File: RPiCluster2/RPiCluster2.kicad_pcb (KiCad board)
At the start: 2 copper layers, 100 x 100 mm, 85 parts, among them J1 RPi_slave_1, J10 Addr_1, J11 Addr_0, J2 RPi_slave_2, J3 RPi_slave_3, J4 RPi_slave_4, J5 Addr, J6 Power_header, J7 Signal_header, J8 Signal_socket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

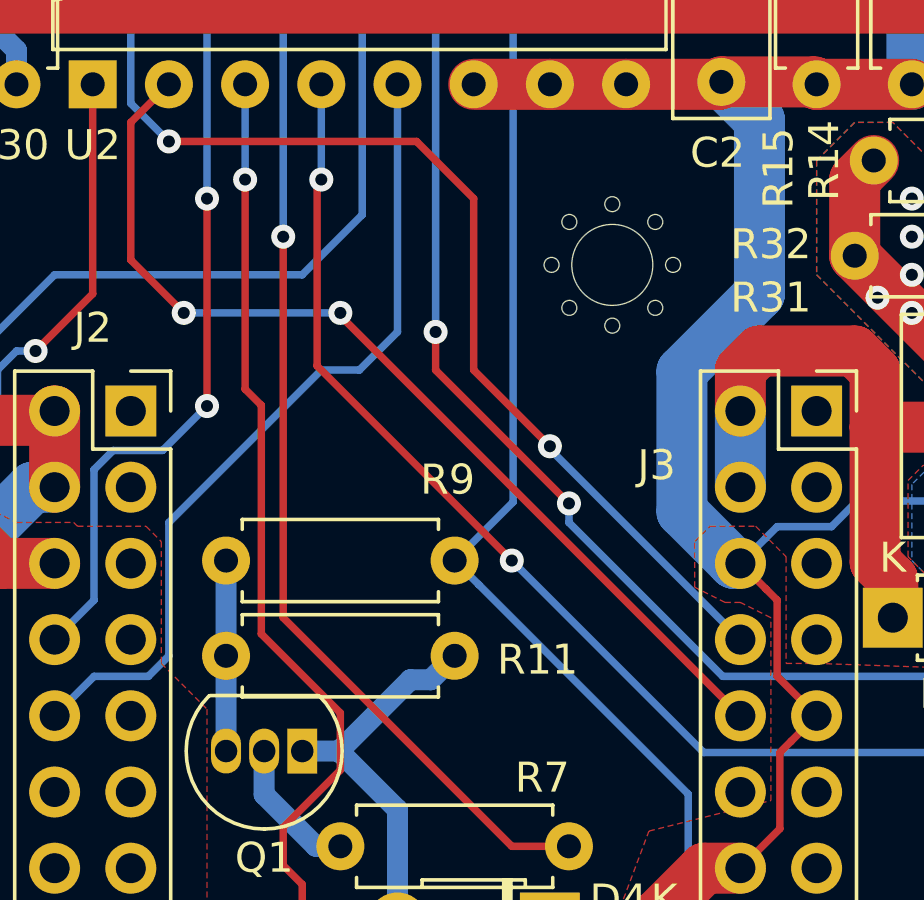
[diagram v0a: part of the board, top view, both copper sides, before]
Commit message: RPiCluster2: Avoid SER_EN from floating so that the board can be tested without MCP23008
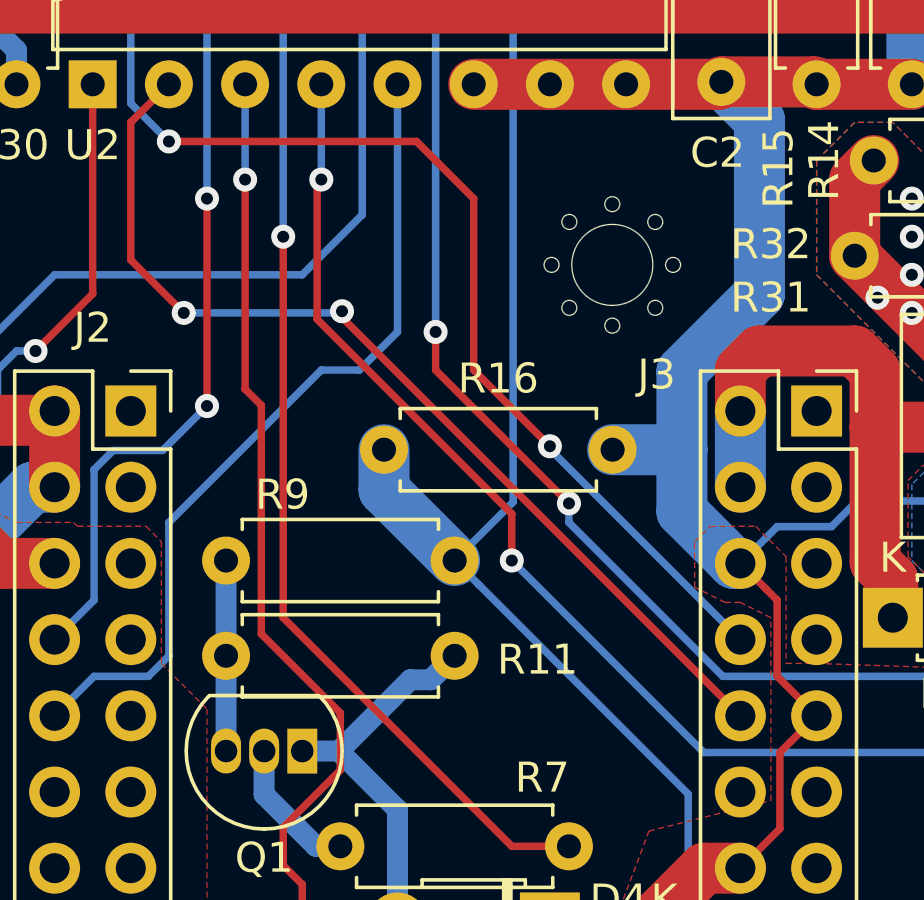
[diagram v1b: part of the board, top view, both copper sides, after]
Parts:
- added R16: 47k, Resistor_THT:R_Axial_DIN0207_L6.3mm_D2.5mm_P7.62mm_Horizontal, F.Cu at (99.9, 96.0)
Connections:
- J1 pad 1: (no net) -> Net-(J1-Pad1)
- J1 pad 11: (no net) -> Net-(J1-Pad11)
- J1 pad 12: (no net) -> Net-(J1-Pad12)
- J1 pad 13: (no net) -> Net-(J1-Pad13)
- J1 pad 15: (no net) -> Net-(J1-Pad15)
- J1 pad 16: (no net) -> Net-(J1-Pad16)
- J1 pad 17: (no net) -> Net-(J1-Pad17)
- J1 pad 18: (no net) -> Net-(J1-Pad18)
- J1 pad 19: (no net) -> Net-(J1-Pad19)
- J1 pad 21: (no net) -> Net-(J1-Pad21)
- J1 pad 22: (no net) -> Net-(J1-Pad22)
- J1 pad 23: (no net) -> Net-(J1-Pad23)
- J1 pad 24: (no net) -> Net-(J1-Pad24)
- J1 pad 26: (no net) -> Net-(J1-Pad26)
- J1 pad 27: (no net) -> Net-(J1-Pad27)
- J1 pad 28: (no net) -> Net-(J1-Pad28)
- J1 pad 29: (no net) -> Net-(J1-Pad29)
- J1 pad 3: (no net) -> Net-(J1-Pad3)
- J1 pad 31: (no net) -> Net-(J1-Pad31)
- J1 pad 32: (no net) -> Net-(J1-Pad32)
- J1 pad 33: (no net) -> Net-(J1-Pad33)
- J1 pad 35: (no net) -> Net-(J1-Pad35)
- J1 pad 36: (no net) -> Net-(J1-Pad36)
- J1 pad 37: (no net) -> Net-(J1-Pad37)
- J1 pad 38: (no net) -> Net-(J1-Pad38)
- J1 pad 40: (no net) -> Net-(J1-Pad40)
- J1 pad 5: (no net) -> Net-(J1-Pad5)
- J1 pad 7: (no net) -> Net-(J1-Pad7)
- J2 pad 1: (no net) -> Net-(J2-Pad1)
- J2 pad 11: (no net) -> Net-(J2-Pad11)
- J2 pad 12: (no net) -> Net-(J2-Pad12)
- J2 pad 13: (no net) -> Net-(J2-Pad13)
- J2 pad 15: (no net) -> Net-(J2-Pad15)
- J2 pad 16: (no net) -> Net-(J2-Pad16)
- J2 pad 17: (no net) -> Net-(J2-Pad17)
- J2 pad 18: (no net) -> Net-(J2-Pad18)
- J2 pad 19: (no net) -> Net-(J2-Pad19)
- J2 pad 21: (no net) -> Net-(J2-Pad21)
- J2 pad 22: (no net) -> Net-(J2-Pad22)
- J2 pad 23: (no net) -> Net-(J2-Pad23)
- J2 pad 24: (no net) -> Net-(J2-Pad24)
- J2 pad 26: (no net) -> Net-(J2-Pad26)
- J2 pad 27: (no net) -> Net-(J2-Pad27)
- J2 pad 28: (no net) -> Net-(J2-Pad28)
- J2 pad 29: (no net) -> Net-(J2-Pad29)
- J2 pad 3: (no net) -> Net-(J2-Pad3)
- J2 pad 31: (no net) -> Net-(J2-Pad31)
- J2 pad 32: (no net) -> Net-(J2-Pad32)
- J2 pad 33: (no net) -> Net-(J2-Pad33)
- J2 pad 35: (no net) -> Net-(J2-Pad35)
- J2 pad 36: (no net) -> Net-(J2-Pad36)
- J2 pad 37: (no net) -> Net-(J2-Pad37)
- J2 pad 38: (no net) -> Net-(J2-Pad38)
- J2 pad 40: (no net) -> Net-(J2-Pad40)
- J2 pad 5: (no net) -> Net-(J2-Pad5)
- J2 pad 7: (no net) -> Net-(J2-Pad7)
- J3 pad 1: (no net) -> Net-(J3-Pad1)
- J3 pad 11: (no net) -> Net-(J3-Pad11)
- J3 pad 12: (no net) -> Net-(J3-Pad12)
- J3 pad 13: (no net) -> Net-(J3-Pad13)
- J3 pad 15: (no net) -> Net-(J3-Pad15)
- J3 pad 16: (no net) -> Net-(J3-Pad16)
- J3 pad 17: (no net) -> Net-(J3-Pad17)
- J3 pad 18: (no net) -> Net-(J3-Pad18)
- J3 pad 19: (no net) -> Net-(J3-Pad19)
- J3 pad 21: (no net) -> Net-(J3-Pad21)
- J3 pad 22: (no net) -> Net-(J3-Pad22)
- J3 pad 23: (no net) -> Net-(J3-Pad23)
- J3 pad 24: (no net) -> Net-(J3-Pad24)
- J3 pad 26: (no net) -> Net-(J3-Pad26)
- J3 pad 27: (no net) -> Net-(J3-Pad27)
- J3 pad 28: (no net) -> Net-(J3-Pad28)
- J3 pad 29: (no net) -> Net-(J3-Pad29)
- J3 pad 3: (no net) -> Net-(J3-Pad3)
- J3 pad 31: (no net) -> Net-(J3-Pad31)
- J3 pad 32: (no net) -> Net-(J3-Pad32)
- J3 pad 33: (no net) -> Net-(J3-Pad33)
- J3 pad 35: (no net) -> Net-(J3-Pad35)
- J3 pad 36: (no net) -> Net-(J3-Pad36)
- J3 pad 37: (no net) -> Net-(J3-Pad37)
- J3 pad 38: (no net) -> Net-(J3-Pad38)
- J3 pad 40: (no net) -> Net-(J3-Pad40)
- J3 pad 5: (no net) -> Net-(J3-Pad5)
- J3 pad 7: (no net) -> Net-(J3-Pad7)
- J4 pad 1: (no net) -> Net-(J4-Pad1)
- J4 pad 11: (no net) -> Net-(J4-Pad11)
- J4 pad 12: (no net) -> Net-(J4-Pad12)
- J4 pad 13: (no net) -> Net-(J4-Pad13)
- J4 pad 15: (no net) -> Net-(J4-Pad15)
- J4 pad 16: (no net) -> Net-(J4-Pad16)
- J4 pad 17: (no net) -> Net-(J4-Pad17)
- J4 pad 18: (no net) -> Net-(J4-Pad18)
- J4 pad 19: (no net) -> Net-(J4-Pad19)
- J4 pad 21: (no net) -> Net-(J4-Pad21)
- J4 pad 22: (no net) -> Net-(J4-Pad22)
- J4 pad 23: (no net) -> Net-(J4-Pad23)
- J4 pad 24: (no net) -> Net-(J4-Pad24)
- J4 pad 26: (no net) -> Net-(J4-Pad26)
- J4 pad 27: (no net) -> Net-(J4-Pad27)
- J4 pad 28: (no net) -> Net-(J4-Pad28)
- J4 pad 29: (no net) -> Net-(J4-Pad29)
- J4 pad 3: (no net) -> Net-(J4-Pad3)
- J4 pad 31: (no net) -> Net-(J4-Pad31)
- J4 pad 32: (no net) -> Net-(J4-Pad32)
- J4 pad 33: (no net) -> Net-(J4-Pad33)
- J4 pad 35: (no net) -> Net-(J4-Pad35)
- J4 pad 36: (no net) -> Net-(J4-Pad36)
- J4 pad 37: (no net) -> Net-(J4-Pad37)
- J4 pad 38: (no net) -> Net-(J4-Pad38)
- J4 pad 40: (no net) -> Net-(J4-Pad40)
- J4 pad 5: (no net) -> Net-(J4-Pad5)
- J4 pad 7: (no net) -> Net-(J4-Pad7)
- U1 pad 17: (no net) -> Net-(U1-Pad17)
- U1 pad 8: (no net) -> Net-(U1-Pad8)
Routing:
- net /SER_EN: track 69.8 -> 74.4 mm
- net GND: track 287.6 -> 289.9 mm

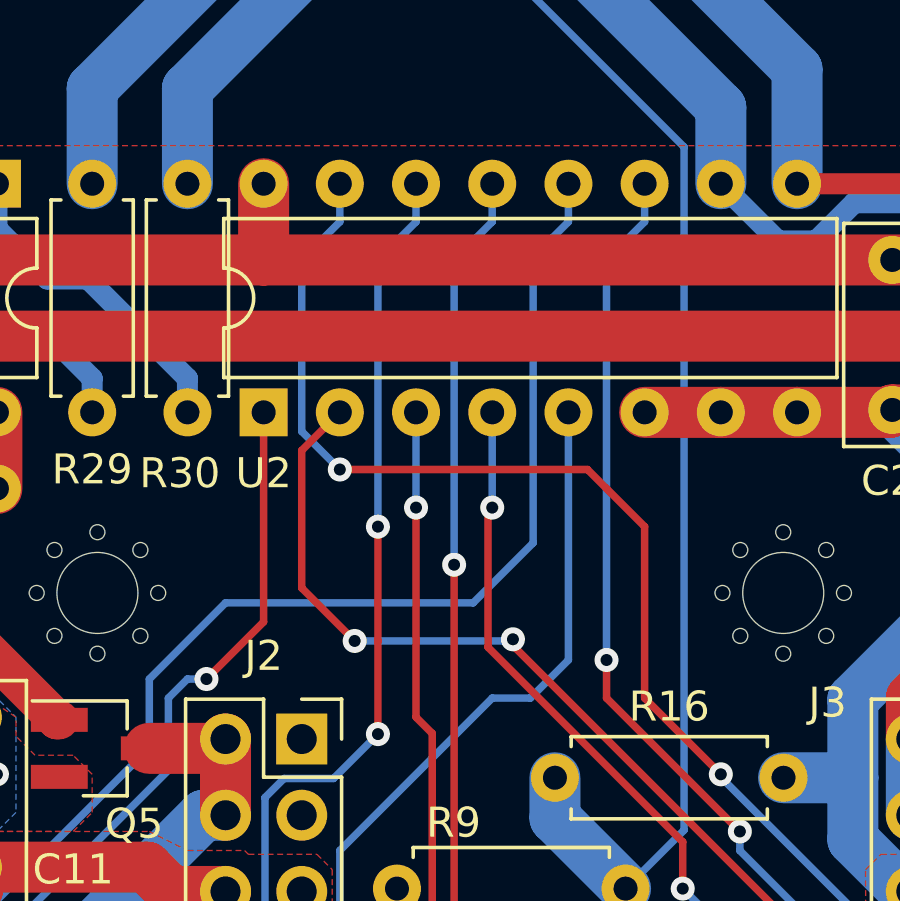
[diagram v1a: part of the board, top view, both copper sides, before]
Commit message: RPiCluster2: Fix swapping slave {TXD,RXD} lines
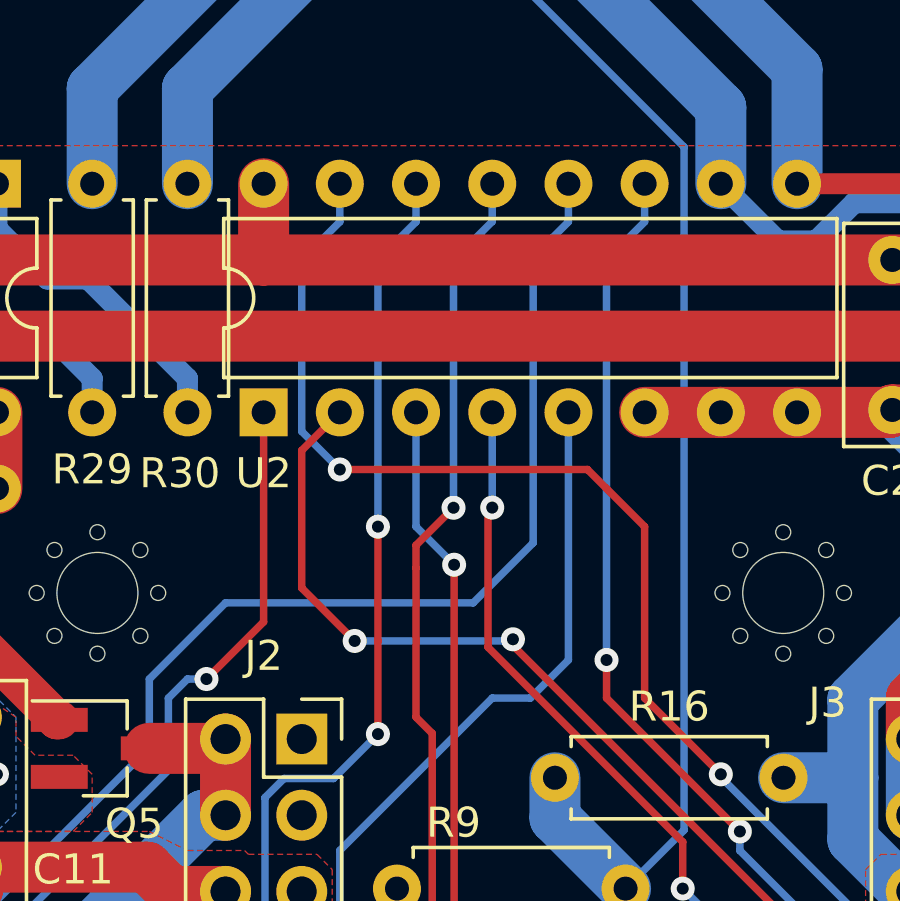
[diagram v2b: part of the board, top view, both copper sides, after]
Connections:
- U2 pad 13: /RXD_SLV -> /TXD_SLV
- U2 pad 3: /TXD_SLV -> /RXD_SLV
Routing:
- net /TXD_SLV: track 47.0 -> 55.6 mm
- net /RXD_SLV: track 38.6 -> 31.0 mm
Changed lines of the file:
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@@
     (thickness 1.6)
     (drawings 10)
-    (tracks 902)
+    (tracks 905)
     (zones 0)
     (modules 86)
@@
       (net 18 /MUX_A))
     (pad 3 thru_hole oval (at 0 5.08 90) (size 1.6 1.6) (drill 0.8) (layers *.Cu *.Mask)
-      (net 19 /TXD_SLV))
+      (net 26 /RXD_SLV))
     (pad 11 thru_hole oval (at 7.62 12.7 90) (size 1.6 1.6) (drill 0.8) (layers *.Cu *.Mask)
       (net 39 /TXD4))
@@
       (net 42 /RXD2))
     (pad 13 thru_hole oval (at 7.62 7.62 90) (size 1.6 1.6) (drill 0.8) (layers *.Cu *.Mask)
-      (net 26 /RXD_SLV))
+      (net 19 /TXD_SLV))
     (pad 6 thru_hole oval (at 0 12.7 90) (size 1.6 1.6) (drill 0.8) (layers *.Cu *.Mask)
       (net 16 GND))
@@
   (segment (start 95.790001 102.140001) (end 95.790001 94.520001) (width 0.25) (layer F.Cu) (net 19))
   (segment (start 98.425 104.775) (end 95.790001 102.140001) (width 0.25) (layer F.Cu) (net 19))
-  (segment (start 95.25 93.98) (end 95.25 86.995) (width 0.25) (layer F.Cu) (net 19))
-  (via (at 95.25 86.995) (size 0.8) (drill 0.4) (layers F.Cu B.Cu) (net 19))
   (segment (start 95.790001 94.520001) (end 95.25 93.98) (width 0.25) (layer F.Cu) (net 19))
-  (segment (start 95.25 86.995) (end 95.25 83.82) (width 0.25) (layer B.Cu) (net 19))
+  (segment (start 95.25 93.98) (end 95.25 89) (width 0.25) (layer F.Cu) (net 19))
+  (via (at 96.5 87) (size 0.8) (drill 0.4) (layers F.Cu B.Cu) (net 19))
+  (segment (start 95.25 88.25) (end 96.5 87) (width 0.25) (layer F.Cu) (net 19))
+  (segment (start 95.25 89) (end 95.25 88.25) (width 0.25) (layer F.Cu) (net 19))
+  (segment (start 96.5 87) (end 96.5 78.75) (width 0.25) (layer B.Cu) (net 19))
+  (segment (start 97.79 77.46) (end 97.79 76.2) (width 0.25) (layer B.Cu) (net 19))
+  (segment (start 96.5 78.75) (end 97.79 77.46) (width 0.25) (layer B.Cu) (net 19))
   (segment (start 97.79 123.825) (end 101.6 123.825) (width 0.7) (layer B.Cu) (net 20))
   (segment (start 101.6 126.365) (end 102.87 127.635) (width 0.7) (layer B.Cu) (net 20))
@@
   (segment (start 92.71 123.875001) (end 85.140001 123.875001) (width 0.25) (layer B.Cu) (net 25))
   (segment (start 106.045 109.22) (end 104.14 109.22) (width 0.25) (layer F.Cu) (net 26))
-  (via (at 96.52 88.9) (size 0.8) (drill 0.4) (layers F.Cu B.Cu) (net 26))
   (segment (start 96.52 101.6) (end 96.52 88.9) (width 0.25) (layer F.Cu) (net 26))
   (segment (start 104.14 109.22) (end 96.52 101.6) (width 0.25) (layer F.Cu) (net 26))
-  (segment (start 96.52 88.9) (end 96.52 78.74) (width 0.25) (layer B.Cu) (net 26))
-  (segment (start 96.52 78.74) (end 97.79 77.47) (width 0.25) (layer B.Cu) (net 26))
-  (segment (start 97.79 77.47) (end 97.79 76.2) (width 0.25) (layer B.Cu) (net 26))
+  (via (at 96.52 88.9) (size 0.8) (drill 0.4) (layers F.Cu B.Cu) (net 26))
+  (segment (start 95.25 87.63) (end 95.25 83.82) (width 0.25) (layer B.Cu) (net 26))
+  (segment (start 96.52 88.9) (end 95.25 87.63) (width 0.25) (layer B.Cu) (net 26))
   (segment (start 97.61 109.22) (end 98.425 109.22) (width 0.7) (layer B.Cu) (net 27))
   (segment (start 95.885 107.495) (end 97.61 109.22) (width 0.7) (layer B.Cu) (net 27))
